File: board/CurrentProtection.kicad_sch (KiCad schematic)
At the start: 26 parts, among them Q4 IPB180N10S4-02, Q9 IPB180N10S4-02, U10 ACS72981LLRATR-100U3, U2 LM5050MK-1_NOPB, U3 LM5050MK-1_NOPB

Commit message: Update CurrentProtection.kicad_sch
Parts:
- R1: value R_US -> 4.7k
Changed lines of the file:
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@@
 			)
 		)
-		(property "Value" "R_US"
+		(property "Value" "4.7k"
 			(at 195.58 95.25 90)
 			(effects

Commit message: added fixes for schematic
redid op amp symbols
put Xs on teensy
Put andersons on current protection page
changed resistor value for buzzer
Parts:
- removed BT1, BT2: Battery, symbol Device:Battery
- added Conn10, Conn11: AndersonPP, symbol MRDT_Connectors:AndersonPP
- R1: value 4.7k -> R_US
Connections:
- net GND: now also Conn10.1 (GND), Conn11.1 (GND)
- net at C5.1, D2.1 (K), Q9.2 (S)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: now also Conn11.4 (PV+)
- net at C11.1, D4.1 (K), Q4.2 (S)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: now also Conn10.4 (PV+)

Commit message: fixed wiring
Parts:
- C2: value C -> 0.1uF
- R1: value R_US -> 4.7k
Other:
- moved on the sheet: C2, Conn10D, Conn11D
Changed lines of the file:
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@@
-	)
-	(junction
-		(at 213.36 109.22)
-		(diameter 0)
-		(color 0 0 0 0)
 	)
 	(junction
@@
 	)
 	(junction
-		(at 213.36 88.9)
+		(at 219.71 88.9)
 		(diameter 0)
 		(color 0 0 0 0)
@@
 	)
 	(junction
-		(at 31.75 83.82)
-		(diameter 0)
-		(color 0 0 0 0)
-	)
-	(junction
 		(at 49.53 111.76)
 		(diameter 0)
@@
 	(junction
 		(at 105.41 170.18)
+		(diameter 0)
+		(color 0 0 0 0)
+	)
+	(junction
+		(at 219.71 109.22)
 		(diameter 0)
 		(color 0 0 0 0)
@@
 	(wire
 		(pts
-			(xy 213.36 109.22) (xy 218.44 109.22)
-		)
-		(stroke
-			(width 0)
-			(type default)
-		)
-	)
-	(wire
-		(pts
 			(xy 52.07 191.77) (xy 52.07 193.04)
 		)
@@
 	(wire
 		(pts
-			(xy 213.36 88.9) (xy 213.36 90.17)
+			(xy 219.71 88.9) (xy 219.71 90.17)
 		)
 		(stroke
@@
 	(wire
 		(pts
-			(xy 29.21 154.94) (xy 34.29 154.94)
+			(xy 29.21 160.02) (xy 34.29 160.02)
 		)
 		(stroke
@@
 	(wire
 		(pts
+			(xy 219.71 109.22) (xy 223.52 109.22)
+		)
+		(stroke
+			(width 0)
+			(type default)
+		)
+	)
+	(wire
+		(pts
 			(xy 199.39 99.06) (xy 200.66 99.06)
 		)
@@
 	(wire
 		(pts
-			(xy 213.36 88.9) (xy 218.44 88.9)
-		)
-		(stroke
-			(width 0)
-			(type default)
-		)
-	)
-	(wire
-		(pts
 			(xy 52.07 181.61) (xy 52.07 182.88)
 		)
@@
 	(wire
 		(pts
-			(xy 29.21 96.52) (xy 29.21 83.82)
+			(xy 31.75 73.66) (xy 31.75 97.79)
 		)
 		(stroke
@@
 	(wire
 		(pts
+			(xy 29.21 97.79) (xy 31.75 97.79)
+		)
+		(stroke
+			(width 0)
+			(type default)
+		)
+	)
+	(wire
+		(pts
 			(xy 55.88 185.42) (xy 55.88 182.88)
 		)
@@
 	(wire
 		(pts
-			(xy 34.29 154.94) (xy 34.29 144.78)
+			(xy 34.29 160.02) (xy 34.29 144.78)
+		)
+		(stroke
+			(width 0)
+			(type default)
+		)
+	)
+	(wire
+		(pts
+			(xy 219.71 88.9) (xy 227.33 88.9)
 		)
 		(stroke
@@
 	(wire
 		(pts
-			(xy 31.75 85.09) (xy 31.75 83.82)
-		)
-		(stroke
-			(width 0)
-			(type default)
-		)
-	)
-	(wire
-		(pts
 			(xy 105.41 144.78) (xy 90.17 144.78)
 		)
@@
 	(wire
 		(pts
-			(xy 218.44 87.63) (xy 218.44 88.9)
-		)
-		(stroke
-			(width 0)
-			(type default)
-		)
-	)
-	(wire
-		(pts
-			(xy 29.21 83.82) (xy 31.75 83.82)
+			(xy 227.33 86.36) (xy 227.33 88.9)
 		)
 		(stroke
@@
 	(wire
 		(pts
-			(xy 180.34 88.9) (xy 213.36 88.9)
+			(xy 180.34 88.9) (xy 219.71 88.9)
 		)
 		(stroke
@@
 	(wire
 		(pts
-			(xy 213.36 97.79) (xy 213.36 109.22)
+			(xy 219.71 97.79) (xy 219.71 109.22)
 		)
 		(stroke
@@
 	(wire
 		(pts
-			(xy 31.75 83.82) (xy 31.75 73.66)
-		)
-		(stroke
-			(width 0)
-			(type default)
-		)
-	)
-	(wire
-		(pts
-			(xy 218.44 109.22) (xy 218.44 110.49)
+			(xy 223.52 109.22) (xy 223.52 110.49)
 		)
 		(stroke
@@
 	(wire
 		(pts
-			(xy 200.66 109.22) (xy 213.36 109.22)
+			(xy 200.66 109.22) (xy 219.71 109.22)
 		)
 		(stroke
@@
 	(symbol
 		(lib_id "MRDT_Connectors:AndersonPP")
-		(at 19.05 99.06 0)
+		(at 19.05 100.33 0)
 		(unit 4)
 		(exclude_from_sim no)
@@
 		(fields_autoplaced yes)
 		(property "Reference" "Conn10"
-			(at 21.59 88.9 0)
+			(at 21.59 90.17 0)
 			(effects
 				(font
@@
 		)
 		(property "Value" "AndersonPP"
-			(at 21.59 91.44 0)
+			(at 21.59 92.71 0)
 			(effects
 				(font
@@
 		)
 		(property "Footprint" ""
-			(at 15.24 113.03 0)
+			(at 15.24 114.3 0)
 			(effects
 				(font
@@
 		)
 		(property "Datasheet" ""
-			(at 15.24 113.03 0)
+			(at 15.24 114.3 0)
 			(effects
 				(font
@@
 		)
 		(property "Description" ""
-			(at 19.05 99.06 0)
+			(at 19.05 100.33 0)
 			(effects
 				(font
@@
 	(symbol
 		(lib_id "power:+3V3")
-		(at 218.44 87.63 0)
+		(at 227.33 86.36 0)
 		(unit 1)
 		(exclude_from_sim no)
@@
 		(fields_autoplaced yes)
 		(property "Reference" "#PWR05"
-			(at 218.44 91.44 0)
+			(at 227.33 90.17 0)
 			(effects
 				(font
@@
 		)
 		(property "Value" "+3V3"
-			(at 218.44 82.55 0)
+			(at 227.33 81.28 0)
 			(effects
 				(font
@@
 		)
 		(property "Footprint" ""
-			(at 218.44 87.63 0)
+			(at 227.33 86.36 0)
 			(effects
 				(font
@@
 		)
 		(property "Datasheet" ""
-			(at 218.44 87.63 0)
+			(at 227.33 86.36 0)
 			(effects
 				(font
@@
 		)
 		(property "Description" "Power symbol creates a global label with name \"+3V3\""
-			(at 218.44 87.63 0)
+			(at 227.33 86.36 0)
 			(effects
 				(font
@@
 	(symbol
 		(lib_id "Device:C")
-		(at 213.36 93.98 0)
+		(at 219.71 93.98 0)
 		(unit 1)
 		(exclude_from_sim no)
@@
 		(fields_autoplaced yes)
 		(property "Reference" "C2"
-			(at 217.17 92.7099 0)
+			(at 223.52 92.7099 0)
 			(effects
 				(font
@@
 			)
 		)
-		(property "Value" "C"
-			(at 217.17 95.2499 0)
+		(property "Value" "0.1uF"
+			(at 223.52 95.2499 0)
 			(effects
 				(font
@@
 		)
 		(property "Footprint" ""
-			(at 214.3252 97.79 0)
+			(at 220.6752 97.79 0)
 			(effects
 				(font
@@
 		)
 		(property "Datasheet" "~"
-			(at 213.36 93.98 0)
+			(at 219.71 93.98 0)
 			(effects
 				(font
@@
 		)
 		(property "Description" "Unpolarized capacitor"
-			(at 213.36 93.98 0)
+			(at 219.71 93.98 0)
 			(effects
 				(font
@@
 	(symbol
 		(lib_id "MRDT_Connectors:AndersonPP")
-		(at 19.05 157.48 0)
+		(at 19.05 162.56 0)
 		(unit 4)
 		(exclude_from_sim no)
@@
 		(fields_autoplaced yes)
 		(property "Reference" "Conn11"
-			(at 21.59 147.32 0)
+			(at 21.59 152.4 0)
 			(effects
 				(font
@@
 		)
 		(property "Value" "AndersonPP"
-			(at 21.59 149.86 0)
+			(at 21.59 154.94 0)
 			(effects
 				(font
@@
 		)
 		(property "Footprint" ""
-			(at 15.24 171.45 0)
+			(at 15.24 176.53 0)
 			(effects
 				(font
@@
 		)
 		(property "Datasheet" ""
-			(at 15.24 171.45 0)
+			(at 15.24 176.53 0)
 			(effects
 				(font
@@
 		)
 		(property "Description" ""
-			(at 19.05 157.48 0)
+			(at 19.05 162.56 0)
 			(effects
 				(font
@@
 	(symbol
 		(lib_id "power:GND")
-		(at 218.44 110.49 0)
+		(at 223.52 110.49 0)
 		(unit 1)
 		(exclude_from_sim no)
@@
 		(fields_autoplaced yes)
 		(property "Reference" "#PWR027"
-			(at 218.44 116.84 0)
+			(at 223.52 116.84 0)
 			(effects
 				(font
@@
 		)
 		(property "Value" "GND"
-			(at 218.44 115.57 0)
+			(at 223.52 115.57 0)
 			(effects
 				(font
@@
 		)
 		(property "Footprint" ""
-			(at 218.44 110.49 0)
+			(at 223.52 110.49 0)
 			(effects
 				(font
@@
 		)
 		(property "Datasheet" ""
-			(at 218.44 110.49 0)
+			(at 223.52 110.49 0)
 			(effects
 				(font
@@
 		)
 		(property "Description" "Power symbol creates a global label with name \"GND\" , ground"
-			(at 218.44 110.49 0)
+			(at 223.52 110.49 0)
 			(effects
 				(font
@@
 			)
 		)
-		(property "Value" "R_US"
+		(property "Value" "4.7k"
 			(at 195.58 95.25 90)
 			(effects

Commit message: Capacitor Change
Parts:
- C1: value 0.1uF -> 1uF
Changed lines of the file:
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@@
 			)
 		)
-		(property "Value" "0.1uF"
+		(property "Value" "1uF"
 			(at 203.454 104.902 0)
 			(effects

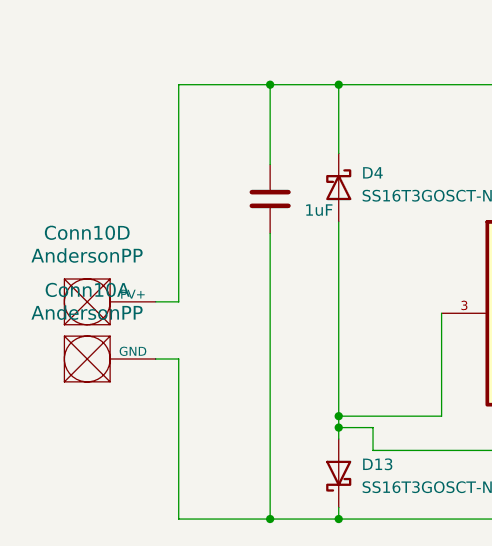
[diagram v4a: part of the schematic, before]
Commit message: added most datasheets [Except Buzzer]
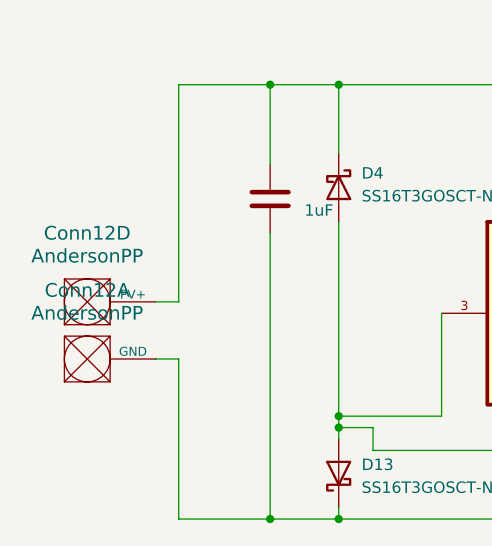
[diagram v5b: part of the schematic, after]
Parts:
- Conn11: footprint (none) -> MRDT_Connectors:Square_Anderson_2_H_Side_By_Side_PV
- Conn12: renamed from Conn10; footprint (none) -> MRDT_Connectors:Square_Anderson_2_H_Side_By_Side_PV
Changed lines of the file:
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@@
 		(dnp no)
 		(fields_autoplaced yes)
-		(property "Reference" "Conn10"
+		(property "Reference" "Conn12"
 			(at 21.59 90.17 0)
 			(effects
@@
 			)
 		)
-		(property "Footprint" ""
+		(property "Footprint" "MRDT_Connectors:Square_Anderson_2_H_Side_By_Side_PV"
 			(at 15.24 114.3 0)
 			(effects
@@
 			(project ""
 				(path "/7eaa639d-7062-45e7-be05-1c2855431307/fa17e088-8bc3-4875-b327-c5ed0adaa270"
-					(reference "Conn10")
+					(reference "Conn12")
 					(unit 4)
 				)
@@
 			)
 		)
-		(property "Footprint" ""
+		(property "Footprint" "MRDT_Connectors:Square_Anderson_2_H_Side_By_Side_PV"
 			(at 15.24 176.53 0)
 			(effects
@@
 		(dnp no)
 		(fields_autoplaced yes)
-		(property "Reference" "Conn10"
+		(property "Reference" "Conn12"
 			(at 21.59 96.52 0)
 			(effects
@@
 			)
 		)
-		(property "Footprint" ""
+		(property "Footprint" "MRDT_Connectors:Square_Anderson_2_H_Side_By_Side_PV"
 			(at 15.24 120.65 0)
 			(effects
@@
 			(project ""
 				(path "/7eaa639d-7062-45e7-be05-1c2855431307/fa17e088-8bc3-4875-b327-c5ed0adaa270"
-					(reference "Conn10")
+					(reference "Conn12")
 					(unit 1)
 				)
@@
 			)
 		)
-		(property "Footprint" ""
+		(property "Footprint" "MRDT_Connectors:Square_Anderson_2_H_Side_By_Side_PV"
 			(at 15.24 187.96 0)
 			(effects

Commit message: More footprints added
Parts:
- C1, C10, C11, C12, C13, C2, C4, C5: footprint (none) -> Capacitor_SMD:C_0603_1608Metric
- D6: footprint (none) -> Diode_SMD:D_0603_1608Metric
- R1, R2, R27, R39: footprint (none) -> Resistor_SMD:R_0603_1608Metric
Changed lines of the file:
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@@
 			)
 		)
-		(property "Footprint" ""
+		(property "Footprint" "Capacitor_SMD:C_0603_1608Metric"
 			(at 220.6752 97.79 0)
 			(effects
@@
 			)
 		)
-		(property "Footprint" ""
+		(property "Footprint" "Capacitor_SMD:C_0603_1608Metric"
 			(at 42.8752 90.17 0)
 			(effects
@@
 			)
 		)
-		(property "Footprint" ""
+		(property "Footprint" "Diode_SMD:D_0603_1608Metric"
 			(at 189.23 142.24 0)
 			(effects
@@
 			)
 		)
-		(property "Footprint" ""
+		(property "Footprint" "Resistor_SMD:R_0603_1608Metric"
 			(at 176.784 141.224 90)
 			(effects
@@
 			)
 		)
-		(property "Footprint" ""
+		(property "Footprint" "Capacitor_SMD:C_0603_1608Metric"
 			(at 199.6948 100.33 0)
 			(effects
@@
 			)
 		)
-		(property "Footprint" ""
+		(property "Footprint" "Capacitor_SMD:C_0603_1608Metric"
 			(at 120.3452 173.99 0)
 			(effects
@@
 			)
 		)
-		(property "Footprint" ""
+		(property "Footprint" "Resistor_SMD:R_0603_1608Metric"
 			(at 195.834 98.044 90)
 			(effects
@@
 			)
 		)
-		(property "Footprint" ""
+		(property "Footprint" "Resistor_SMD:R_0603_1608Metric"
 			(at 101.854 92.456 90)
 			(effects
@@
 			)
 		)
-		(property "Footprint" ""
+		(property "Footprint" "Capacitor_SMD:C_0603_1608Metric"
 			(at 117.8052 102.87 0)
 			(effects
@@
 			)
 		)
-		(property "Footprint" ""
+		(property "Footprint" "Capacitor_SMD:C_0603_1608Metric"
 			(at 103.8352 114.3 0)
 			(effects
@@
 			)
 		)
-		(property "Footprint" ""
+		(property "Footprint" "Resistor_SMD:R_0603_1608Metric"
 			(at 104.394 163.576 90)
 			(effects
@@
 			)
 		)
-		(property "Footprint" ""
+		(property "Footprint" "Capacitor_SMD:C_0603_1608Metric"
 			(at 106.3752 185.42 0)
 			(effects
@@
 			)
 		)
-		(property "Footprint" ""
+		(property "Footprint" "Capacitor_SMD:C_0603_1608Metric"
 			(at 45.4152 161.29 0)
 			(effects

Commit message: Changed footprints to handsolder version
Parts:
- C1, C10, C11, C12, C13, C2, C4, C5: footprint Capacitor_SMD:C_0603_1608Metric -> Capacitor_SMD:C_0603_1608Metric_Pad1.08x0.95mm_HandSolder
- D6: footprint Diode_SMD:D_0603_1608Metric -> LED_SMD:LED_0603_1608Metric_Pad1.05x0.95mm_HandSolder
- R1, R2, R27, R39: footprint Resistor_SMD:R_0603_1608Metric -> Resistor_SMD:R_0603_1608Metric_Pad0.98x0.95mm_HandSolder
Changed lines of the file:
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@@
 			)
 		)
-		(property "Footprint" "Capacitor_SMD:C_0603_1608Metric"
+		(property "Footprint" "Capacitor_SMD:C_0603_1608Metric_Pad1.08x0.95mm_HandSolder"
 			(at 220.6752 97.79 0)
 			(effects
@@
 			)
 		)
-		(property "Footprint" "Capacitor_SMD:C_0603_1608Metric"
+		(property "Footprint" "Capacitor_SMD:C_0603_1608Metric_Pad1.08x0.95mm_HandSolder"
 			(at 42.8752 90.17 0)
 			(effects
@@
 			)
 		)
-		(property "Footprint" "Diode_SMD:D_0603_1608Metric"
+		(property "Footprint" "LED_SMD:LED_0603_1608Metric_Pad1.05x0.95mm_HandSolder"
 			(at 189.23 142.24 0)
 			(effects
@@
 			)
 		)
-		(property "Footprint" "Resistor_SMD:R_0603_1608Metric"
+		(property "Footprint" "Resistor_SMD:R_0603_1608Metric_Pad0.98x0.95mm_HandSolder"
 			(at 176.784 141.224 90)
 			(effects
@@
 			)
 		)
-		(property "Footprint" "Capacitor_SMD:C_0603_1608Metric"
+		(property "Footprint" "Capacitor_SMD:C_0603_1608Metric_Pad1.08x0.95mm_HandSolder"
 			(at 199.6948 100.33 0)
 			(effects
@@
 			)
 		)
-		(property "Footprint" "Capacitor_SMD:C_0603_1608Metric"
+		(property "Footprint" "Capacitor_SMD:C_0603_1608Metric_Pad1.08x0.95mm_HandSolder"
 			(at 120.3452 173.99 0)
 			(effects
@@
 			)
 		)
-		(property "Footprint" "Resistor_SMD:R_0603_1608Metric"
+		(property "Footprint" "Resistor_SMD:R_0603_1608Metric_Pad0.98x0.95mm_HandSolder"
 			(at 195.834 98.044 90)
 			(effects
@@
 			)
 		)
-		(property "Footprint" "Resistor_SMD:R_0603_1608Metric"
+		(property "Footprint" "Resistor_SMD:R_0603_1608Metric_Pad0.98x0.95mm_HandSolder"
 			(at 101.854 92.456 90)
 			(effects
@@
 			)
 		)
-		(property "Footprint" "Capacitor_SMD:C_0603_1608Metric"
+		(property "Footprint" "Capacitor_SMD:C_0603_1608Metric_Pad1.08x0.95mm_HandSolder"
 			(at 117.8052 102.87 0)
 			(effects
@@
 			)
 		)
-		(property "Footprint" "Capacitor_SMD:C_0603_1608Metric"
+		(property "Footprint" "Capacitor_SMD:C_0603_1608Metric_Pad1.08x0.95mm_HandSolder"
 			(at 103.8352 114.3 0)
 			(effects
@@
 			)
 		)
-		(property "Footprint" "Resistor_SMD:R_0603_1608Metric"
+		(property "Footprint" "Resistor_SMD:R_0603_1608Metric_Pad0.98x0.95mm_HandSolder"
 			(at 104.394 163.576 90)
 			(effects
@@
 			)
 		)
-		(property "Footprint" "Capacitor_SMD:C_0603_1608Metric"
+		(property "Footprint" "Capacitor_SMD:C_0603_1608Metric_Pad1.08x0.95mm_HandSolder"
 			(at 106.3752 185.42 0)
 			(effects
@@
 			)
 		)
-		(property "Footprint" "Capacitor_SMD:C_0603_1608Metric"
+		(property "Footprint" "Capacitor_SMD:C_0603_1608Metric_Pad1.08x0.95mm_HandSolder"
 			(at 45.4152 161.29 0)
 			(effects

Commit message: Final footprints added
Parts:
- U2, U3: footprint LM5050MK-1_NOPB:SOT95P280X110-6N -> PowerManagementBoard:SOT95P280X110-6N
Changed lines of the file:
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@@
 			)
 		)
-		(property "Footprint" "LM5050MK-1_NOPB:SOT95P280X110-6N"
+		(property "Footprint" "PowerManagementBoard:SOT95P280X110-6N"
 			(at 78.74 99.06 0)
 			(effects
@@
 			)
 		)
-		(property "Footprint" "LM5050MK-1_NOPB:SOT95P280X110-6N"
+		(property "Footprint" "PowerManagementBoard:SOT95P280X110-6N"
 			(at 81.28 170.18 0)
 			(effects
